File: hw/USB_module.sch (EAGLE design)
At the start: 39 parts, among them J1 GROVE-4P-2.0-3470130P1, J2 GROVE-4P-2.0-3470130P1, J4 MICRO-USB-5P-340015001, X5 53047-04

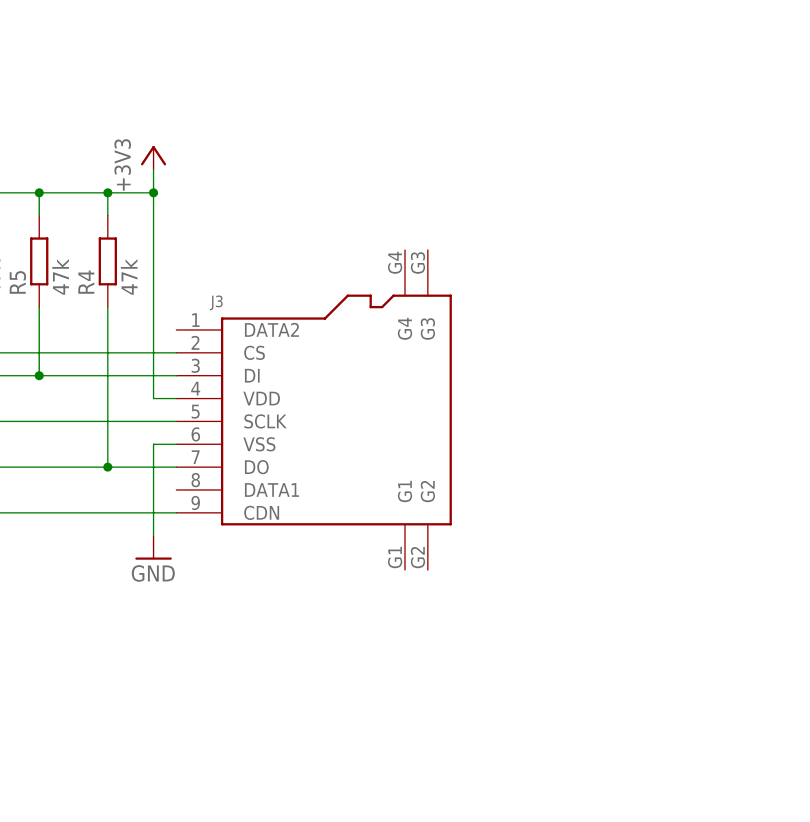
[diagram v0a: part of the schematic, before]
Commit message: Grounded uSD shield
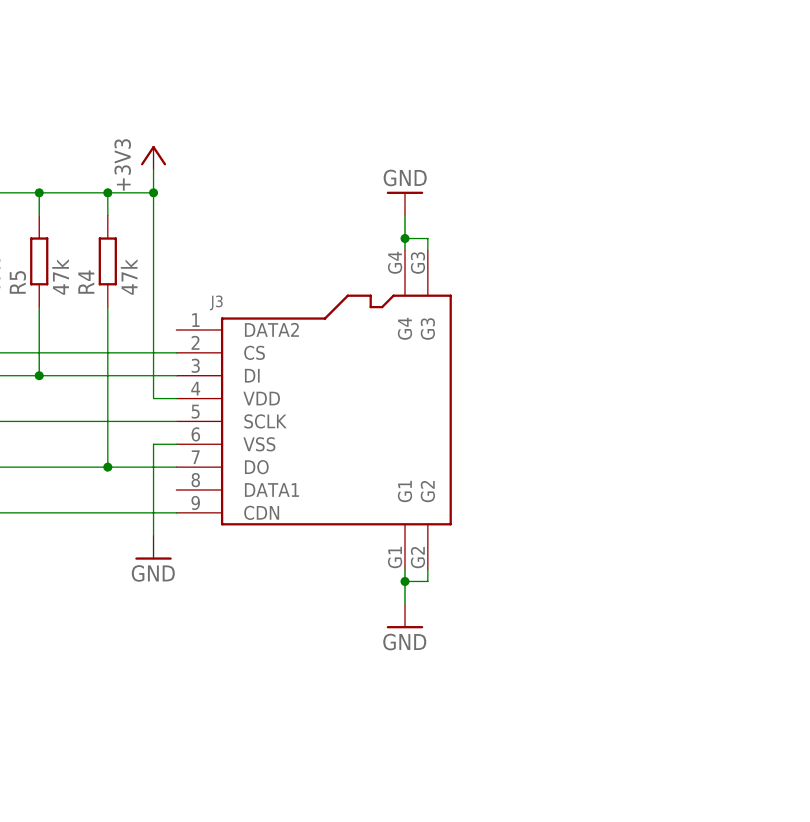
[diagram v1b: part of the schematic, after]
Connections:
- net GND: now also J3.G1, J3.G2, J3.G3, J3.G4
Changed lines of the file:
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@@
 <part name="R6" library="rcl" deviceset="R-EU_" device="R0603" value="330"/>
 <part name="GND23" library="supply" deviceset="GND" device=""/>
+<part name="GND24" library="supply1" deviceset="GND" device=""/>
+<part name="GND26" library="supply1" deviceset="GND" device=""/>
 </parts>
 <sheets>
@@
 <instance part="R6" gate="G$1" x="254" y="101.6" rot="R90"/>
 <instance part="GND23" gate="1" x="254" y="83.82"/>
+<instance part="GND24" gate="1" x="342.9" y="96.52"/>
+<instance part="GND26" gate="1" x="342.9" y="144.78" rot="R180"/>
 </instances>
 <busses>
@@
 <pinref part="LED2" gate="G$1" pin="C"/>
 </segment>
+<segment>
+<pinref part="GND26" gate="1" pin="GND"/>
+<wire x1="345.44" y1="139.7" x2="342.9" y2="139.7" width="0.1524" layer="91"/>
+<wire x1="342.9" y1="139.7" x2="342.9" y2="142.24" width="0.1524" layer="91"/>
+<pinref part="J3" gate="G$1" pin="G3"/>
+<wire x1="345.44" y1="138.43" x2="345.44" y2="139.7" width="0.1524" layer="91"/>
+<pinref part="J3" gate="G$1" pin="G4"/>
+<wire x1="342.9" y1="138.43" x2="342.9" y2="139.7" width="0.1524" layer="91"/>
+<junction x="342.9" y="139.7"/>
+</segment>
+<segment>
+<pinref part="GND24" gate="1" pin="GND"/>
+<pinref part="J3" gate="G$1" pin="G1"/>
+<wire x1="342.9" y1="99.06" x2="342.9" y2="101.6" width="0.1524" layer="91"/>
+<pinref part="J3" gate="G$1" pin="G2"/>
+<wire x1="342.9" y1="101.6" x2="342.9" y2="102.87" width="0.1524" layer="91"/>
+<wire x1="345.44" y1="102.87" x2="345.44" y2="101.6" width="0.1524" layer="91"/>
+<wire x1="345.44" y1="101.6" x2="342.9" y2="101.6" width="0.1524" layer="91"/>
+<junction x="342.9" y="101.6"/>
+</segment>
 </net>
